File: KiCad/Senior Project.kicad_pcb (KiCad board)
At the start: 4 copper layers, 25 x 60 mm, 86 parts, among them J1 USB_C_Receptacle_USB2.0_16P, J2 Screw_Terminal_01x02, J3 Screw_Terminal_01x06, J4 Conn_ARM_JTAG_SWD_10, J5 Conn_01x02, Q2 IRLML0030, Q3 IRLML0030, Q4 IRLML0030, SW1 SW_Push, SW2 SW_Push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

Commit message: 3d model fixes
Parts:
- U4: value MS560702BA03-50 -> e
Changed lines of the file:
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@@
 		)
 		(embedded_fonts no)
+		(model "${KIPRJMOD}/3dmodels/IND_TAIYO_NR3015_TAY.step"
+			(offset
+				(xyz 0 0 0)
+			)
+			(scale
+				(xyz 1 1 1)
+			)
+			(rotate
+				(xyz -0 -0 -0)
+			)
+		)
 	)
 	(footprint "S3FH4R2:QFN40P700X700X90-57N"
@@
 		)
 		(embedded_fonts no)
+		(model "${KIPRJMOD}/3dmodels/ESP32-S3FH4R2.step"
+			(offset
+				(xyz 0 0 0)
+			)
+			(scale
+				(xyz 1 1 1)
+			)
+			(rotate
+				(xyz -90 -0 -0)
+			)
+		)
 	)
 	(footprint "Capacitor_SMD:C_0402_1005Metric"
@@
 		)
 		(embedded_fonts no)
-		(model "${KICAD9_3DMODEL_DIR}/Button_Switch_SMD.3dshapes/SW_SPST_PTS810.wrl"
+		(model "${KIPRJMOD}/3dmodels/PTS810SJM250SMTR LFS.STEP"
 			(offset
 				(xyz 0 0 0)
@@
 			)
 			(rotate
-				(xyz 0 0 0)
+				(xyz -90 -0 -0)
 			)
 		)
@@
 		)
 		(embedded_fonts no)
-		(model "${KICAD9_3DMODEL_DIR}/Button_Switch_SMD.3dshapes/SW_SPST_PTS810.wrl"
+		(model "${KIPRJMOD}/3dmodels/PTS810SJM250SMTR LFS.STEP"
 			(offset
 				(xyz 0 0 0)
@@
 			)
 			(rotate
-				(xyz 0 0 0)
+				(xyz -90 -0 -0)
 			)
 		)
@@
 			)
 		)
-		(property "Value" "MS560702BA03-50"
+		(property "Value" "e"
 			(at 0 0 0)
 			(unlocked yes)
@@
 		)
 		(embedded_fonts no)
+		(model "${KIPRJMOD}/3dmodels/MS560702BA03-50.STEP"
+			(offset
+				(xyz 0 0 1)
+			)
+			(scale
+				(xyz 1 1 1)
+			)
+			(rotate
+				(xyz -0 -0 -90)
+			)
+		)
 	)
 	(footprint "Resistor_SMD:R_0402_1005Metric"
@@
 		)
 		(embedded_fonts no)
-		(model "${KICAD9_3DMODEL_DIR}/RF_Module.3dshapes/HOPERF_RFM9XW_SMD.wrl"
+		(model "${KIPRJMOD}/3dmodels/RFM95W-915S2.STEP"
 			(offset
 				(xyz 0 0 0)
@@
 			)
 			(rotate
-				(xyz 0 0 0)
+				(xyz -90 -0 -0)
 			)
 		)
@@
 		)
 		(embedded_fonts no)
-		(model "${KICAD9_3DMODEL_DIR}/RF_Antenna.3dshapes/Molex_47948-0001_2.4Ghz.wrl"
+		(model "${KIPRJMOD}/3dmodels/0479480001.step"
 			(offset
-				(xyz 0 0 0)
+				(xyz 0 0 4)
 			)
 			(scale
@@
 			)
 			(rotate
-				(xyz 0 0 0)
+				(xyz -0 180 90)
 			)
 		)
@@
 		)
 		(embedded_fonts no)
-		(model "${KICAD9_3DMODEL_DIR}/RF_GPS.3dshapes/ublox_SAM-M8Q.wrl"
+		(model "${KIPRJMOD}/3dmodels/SAM-M10Q-00B.STEP"
 			(offset
 				(xyz 0 0 0)
@@
 			)
 			(rotate
-				(xyz 0 0 0)
+				(xyz -90 -0 -0)
 			)
 		)

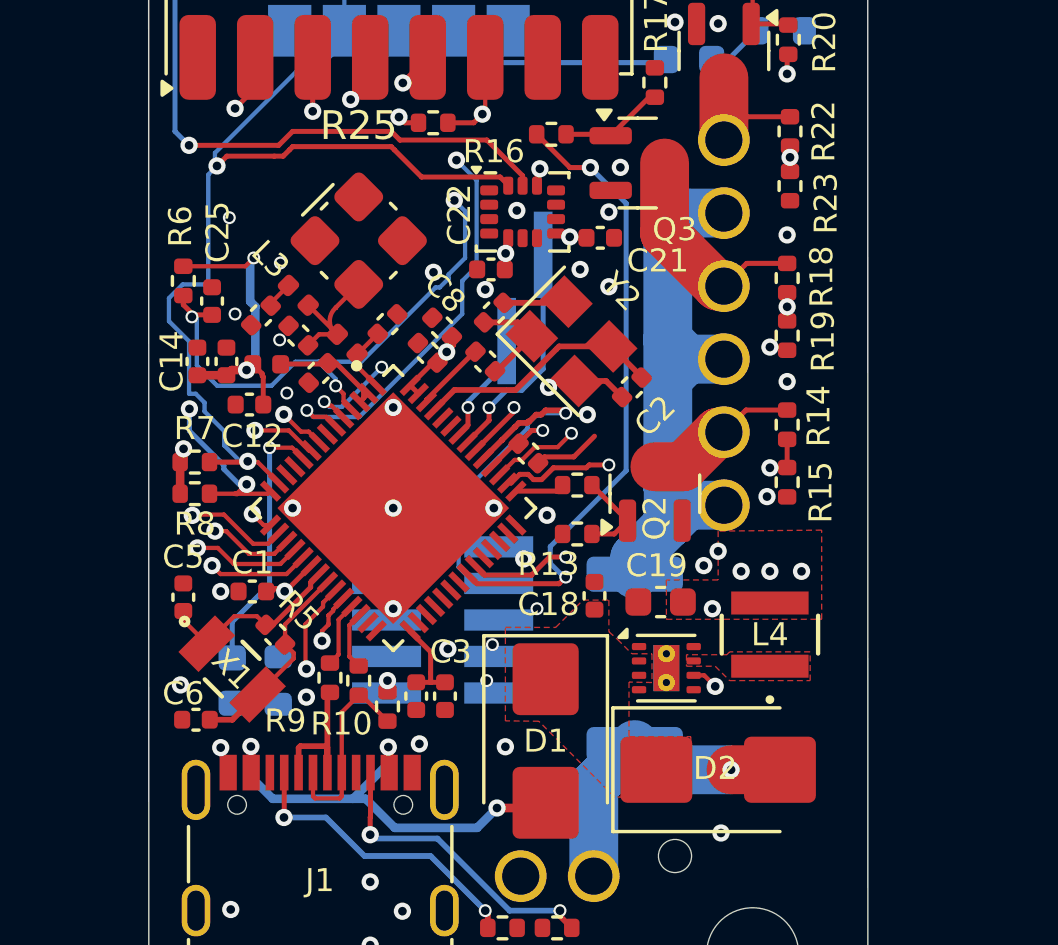
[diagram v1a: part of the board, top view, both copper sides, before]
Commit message: clean up schematic, add voltage dividers for measuring battery and charge firing current
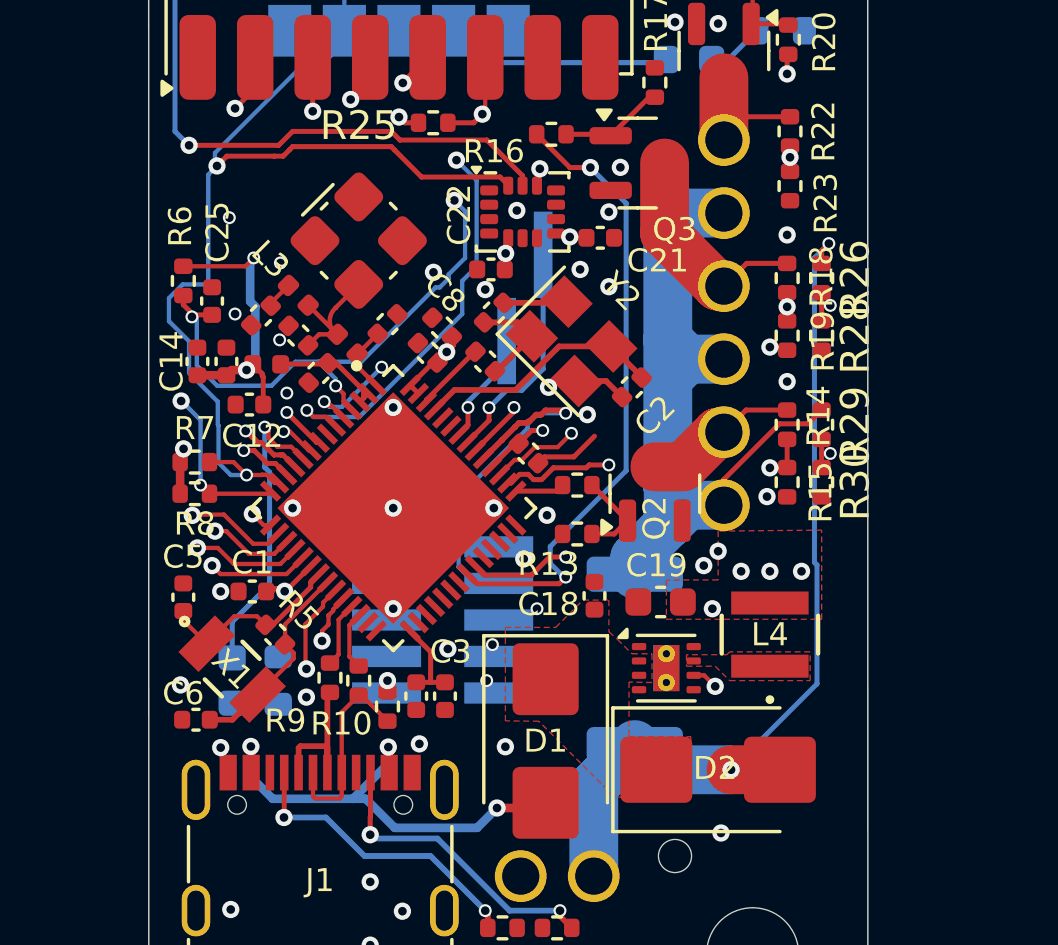
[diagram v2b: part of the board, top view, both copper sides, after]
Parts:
- added R26: 33k, Resistor_SMD:R_0402_1005Metric, F.Cu at (98.4, 89.5)
- added R28: 10k, Resistor_SMD:R_0402_1005Metric, F.Cu at (98.4, 91.5)
- added R29: 33k, Resistor_SMD:R_0402_1005Metric, F.Cu at (98.4, 94.6)
- added R30: 10k, Resistor_SMD:R_0402_1005Metric, F.Cu at (98.4, 96.6)
- U4: value e -> MS560702BA03-50
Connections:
- net /ESP-32 Power Coupler/VDD3P3 renamed Net-(U1-VDD3P3)
- net /LNA Shield/LNA_IN renamed /WiFi Antenna/LNA_IN
- net Net-(JP2-B) renamed /BOOT
- C3 pad 1: Net-(U1-VDD_SPI) -> +3V3
- C7 pad 1: Net-(U1-VDD_SPI) -> +3V3
- U1 pad 11: unconnected-(U1-GPIO6-Pad11) -> /BATTERY_SENSE
- U1 pad 12: unconnected-(U1-GPIO7-Pad12) -> /CURRENT_SENSE
- U1 pad 29: Net-(U1-VDD_SPI) -> +3V3
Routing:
- net /CURRENT_SENSE: track 0.00 -> 27.2 mm, vias 0 -> 2
- net /BATTERY_SENSE: track 0.00 -> 26.6 mm, vias 0 -> 2
- net +BATT: track 11.9 -> 32.4 mm, vias 1 -> 2
- net Net-(J3-Pin_1): track 21.0 -> 26.3 mm
- net Net-(U1-VDD_SPI): track 3.09 -> 0.00 mm
- net +3V3: track 69.0 -> 72.1 mm
- net /RADIO_RST: track 21.7 -> 19.8 mm
- net /POWER_LED: track 9.17 -> 10.6 mm
- net /SCL: track 65.1 -> 64.2 mm
- net /SDA: track 59.4 -> 58.6 mm
- net /FSPICS0: track 20.3 -> 20.8 mm

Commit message: finalize layout, again
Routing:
- net /SDA: track 58.6 -> 58.0 mm
- net GND: vias 62 -> 64
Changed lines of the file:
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@@
 		(tags "resistor")
 		(property "Reference" "R30"
-			(at 0 -1.17 90)
+			(at 2 0 90)
 			(layer "F.SilkS")
 			(effects
 				(font
-					(size 1 1)
+					(size 0.8 0.8)
 					(thickness 0.15)
 				)
@@
 		(tags "resistor")
 		(property "Reference" "R29"
-			(at 0 -1.17 90)
+			(at -0.35 -0.95 270)
 			(layer "F.SilkS")
 			(effects
 				(font
-					(size 1 1)
+					(size 0.8 0.8)
 					(thickness 0.15)
 				)
@@
 		(tags "resistor")
 		(property "Reference" "R23"
-			(at 0.6 -1.25 90)
+			(at 0.35 -1.2 90)
 			(layer "F.SilkS")
 			(effects
@@
 		(tags "resistor")
 		(property "Reference" "R26"
-			(at 0 -1.17 90)
+			(at -0.4 -0.95 90)
 			(layer "F.SilkS")
 			(effects
 				(font
-					(size 1 1)
+					(size 0.8 0.8)
 					(thickness 0.15)
 				)
@@
 		(tags "resistor")
 		(property "Reference" "R19"
-			(at 0.2 -1.25 90)
+			(at 0.25 0.9 90)
 			(layer "F.SilkS")
 			(effects
 				(font
-					(size 0.8 0.8)
+					(size 0.6 0.8)
 					(thickness 0.15)
 				)
@@
 			(effects
 				(font
-					(size 1 1)
+					(size 0.8 0.8)
 					(thickness 0.15)
 				)
@@
 		(tags "resistor")
 		(property "Reference" "R15"
-			(at 0.35 -1.17 90)
+			(at 2 0 270)
 			(layer "F.SilkS")
 			(effects
@@
 			(effects
 				(font
-					(size 1 1)
+					(size 0.8 0.8)
 					(thickness 0.15)
 				)
@@
 		(tags "resistor")
 		(property "Reference" "R28"
-			(at 0 -1.17 90)
+			(at 0.45 -0.95 90)
 			(layer "F.SilkS")
 			(effects
 				(font
-					(size 1 1)
+					(size 0.8 0.8)
 					(thickness 0.15)
 				)
@@
 		(tags "resistor")
 		(property "Reference" "R14"
-			(at -0.3 -1.1 90)
+			(at 0 0.9 270)
 			(layer "F.SilkS")
 			(effects
 				(font
-					(size 0.8 0.8)
+					(size 0.6 0.8)
 					(thickness 0.15)
 				)
@@
 		(tags "resistor")
 		(property "Reference" "R18"
-			(at -0.05 -1.2 90)
+			(at 0 0.9 90)
 			(layer "F.SilkS")
 			(effects
 				(font
-					(size 0.8 0.8)
+					(size 0.6 0.8)
 					(thickness 0.15)
 				)
@@
 		(effects
 			(font
-				(size 1 1)
+				(size 0.8 0.8)
 				(thickness 0.15)
 			)
@@
 		(effects
 			(font
-				(size 1 1)
+				(size 0.8 0.8)
 				(thickness 0.15)
 			)
@@
 	)
 	(via
+		(at 76.4 85.75)
+		(size 0.45)
+		(drill 0.3)
+		(layers "F.Cu" "B.Cu")
+		(free yes)
+		(net 2)
+	)
+	(via
 		(at 80.480264 104.074525)
 		(size 0.6)
@@
 	)
 	(via
+		(at 75.7 99.2)
+		(size 0.45)
+		(drill 0.3)
+		(layers "F.Cu" "B.Cu")
+		(free yes)
+		(net 2)
+	)
+	(via
 		(at 88.3 76.5)
 		(size 0.6)
@@
 	)
 	(segment
-		(start 77.4 93.8)
-		(end 76.4 92.8)
+		(start 77.85 96.35)
+		(end 77.425 95.925)
 		(width 0.15)
 		(layer "B.Cu")
@@
 	)
 	(segment
-		(start 77.0677 85.904602)
-		(end 77.371702 85.6006)
+		(start 81.8 80.9)
+		(end 81.8 79.5)
 		(width 0.15)
 		(layer "B.Cu")
@@
 	(segment
 		(start 76.178878 89.721122)
-		(end 77.021122 89.721122)
-		(width 0.15)
-		(layer "B.Cu")
-		(net 28)
-	)
-	(segment
-		(start 78.4 96.35)
-		(end 77.85 96.35)
+		(end 76.25 89.721122)
 		(width 0.15)
 		(layer "B.Cu")
@@
 	)
 	(segment
-		(start 77.85 96.35)
-		(end 77.425 95.925)
+		(start 81.024 82.076)
+		(end 81.8 81.3)
 		(width 0.15)
 		(layer "B.Cu")
@@
 	)
 	(segment
-		(start 75.7 90.2)
+		(start 75.9 90)
 		(end 76.178878 89.721122)
 		(width 0.15)
@@
 	(segment
 		(start 76.4 91.7)
-		(end 75.7 91)
+		(end 75.9 91.2)
 		(width 0.15)
 		(layer "B.Cu")
@@
 	)
 	(segment
-		(start 81.8 80.9)
-		(end 81.8 79.5)
+		(start 81.8 81.3)
+		(end 81.8 80.9)
 		(width 0.15)
 		(layer "B.Cu")
@@
 	)
 	(segment
-		(start 75.7 91)
-		(end 75.7 90.2)
+		(start 81.8 79.5)
+		(end 83.6 77.7)
 		(width 0.15)
 		(layer "B.Cu")
@@
 	)
 	(segment
-		(start 77.0677 89.674543)
-		(end 77.0677 85.904602)
+		(start 78.4 96.35)
+		(end 77.85 96.35)
 		(width 0.15)
 		(layer "B.Cu")
@@
 	)
 	(segment
-		(start 81.024 82.076)
-		(end 81.8 81.3)
+		(start 77.3 85.1477)
+		(end 80.3717 82.076)
 		(width 0.15)
 		(layer "B.Cu")
@@
 	)
 	(segment
-		(start 76.4 92.8)
-		(end 76.4 91.7)
-		(width 0.15)
+		(start 77.3 85.6006)
+		(end 77.371702 85.6006)
+		(width 0.175)
 		(layer "B.Cu")
 		(net 28)
 	)
 	(segment
-		(start 81.8 81.3)
-		(end 81.8 80.9)
+		(start 77.3 85.6006)
+		(end 77.3 85.1477)
 		(width 0.15)
 		(layer "B.Cu")
@@
 	)
 	(segment
-		(start 81.8 79.5)
-		(end 83.6 77.7)
+		(start 76.25 86.722302)
+		(end 77.371702 85.6006)
 		(width 0.15)
 		(layer "B.Cu")
@@
 	)
 	(segment
-		(start 77.3 85.1477)
-		(end 80.3717 82.076)
+		(start 76.25 89.721122)
+		(end 76.25 86.722302)
 		(width 0.15)
 		(layer "B.Cu")
@@
 	)
 	(segment
-		(start 77.3 85.6006)
-		(end 77.371702 85.6006)
-		(width 0.175)
+		(start 76.4 92.8)
+		(end 76.4 91.7)
+		(width 0.15)
 		(layer "B.Cu")
 		(net 28)
 	)
 	(segment
-		(start 77.3 85.6006)
-		(end 77.3 85.1477)
+		(start 75.9 91.2)
+		(end 75.9 90)
 		(width 0.15)
 		(layer "B.Cu")
@@
 	)
 	(segment
-		(start 77.021122 89.721122)
-		(end 77.0677 89.674543)
+		(start 77.4 93.8)
+		(end 76.4 92.8)
 		(width 0.15)
 		(layer "B.Cu")

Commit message: ordering, for real this time
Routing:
- net +3V3: track 72.1 -> 73.1 mm, vias 20 -> 21
- net GND: vias 64 -> 63
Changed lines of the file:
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@@
 		(end 99.000139 60)
 		(stroke
-			(width 0.05)
+			(width 0.001)
 			(type default)
 		)
@@
 		(end 100.007346 113)
 		(stroke
-			(width 0.05)
+			(width 0.001)
 			(type default)
 		)
@@
 	)
 	(gr_line
-		(start 92.11943 113.999999)
-		(end 75.999861 114)
+		(start 92.119569 113.999999)
+		(end 76 114)
 		(stroke
-			(width 0.05)
+			(width 0.001)
 			(type default)
 		)
@@
 	(gr_arc
 		(start 100.007346 113)
-		(mid 96.504002 116.975526)
-		(end 92.11943 114)
+		(mid 96.504019 116.975523)
+		(end 92.119439 114.000033)
 		(stroke
-			(width 0.05)
+			(width 0.001)
 			(type default)
 		)
@@
 		(end 100.000139 60.999861)
 		(stroke
-			(width 0.05)
+			(width 0.001)
 			(type default)
 		)
@@
 	)
 	(gr_line
-		(start 74.999861 113.000139)
-		(end 74.992654 61)
+		(start 75 113)
+		(end 74.992793 60.999861)
 		(stroke
-			(width 0.05)
+			(width 0.001)
 			(type default)
 		)
@@
 	)
 	(gr_arc
-		(start 75.999861 114)
-		(mid 75.292803 113.707156)
-		(end 74.999861 113.000139)
+		(start 75.9999 114)
+		(mid 75.292793 113.707107)
+		(end 74.9999 113)
 		(stroke
-			(width 0.05)
+			(width 0.001)
 			(type default)
 		)
@@
 		(end 82.88057 60)
 		(stroke
-			(width 0.05)
+			(width 0.001)
 			(type default)
 		)
@@
 		(layer "Cmts.User")
 		(pts
-			(xy 75 114) (xy 75 60)
-		)
-		(height -6.3)
-		(orientation 1)
-		(format
-			(prefix "")
-			(suffix "")
-			(units 3)
-			(units_format 0)
-			(precision 4)
-			(suppress_zeroes yes)
-		)
-		(style
-			(thickness 0.1)
-			(arrow_length 1.27)
-			(text_position_mode 0)
-			(arrow_direction outward)
-			(extension_height 0.58642)
-			(extension_offset 0.5)
-			(keep_text_aligned yes)
-		)
-		(gr_text "54"
-			(at 67.55 87 90)
-			(layer "Cmts.User")
-			(effects
-				(font
-					(size 1 1)
-					(thickness 0.15)
-				)
-			)
-		)
-	)
-	(dimension
-		(type orthogonal)
-		(layer "Cmts.User")
-		(pts
-			(xy 75 114) (xy 100 114)
+			(xy 74.999901 113.000139) (xy 100 114)
 		)
 		(height 8)
@@
 			(keep_text_aligned yes)
 		)
-		(gr_text "25"
-			(at 87.5 120.85 0)
+		(gr_text "25.0001"
+			(at 87.499951 119.850139 0)
 			(layer "Cmts.User")
 			(effects
@@
 		(layer "Cmts.User")
 		(pts
-			(xy 78.9 56.99) (xy 95.9 117)
+			(xy 78.997179 56.992655) (xy 95.988967 117.007331)
 		)
 		(height -18.18)
@@
 			(keep_text_aligned yes)
 		)
-		(gr_text "60.01"
-			(at 59.57 86.995 90)
+		(gr_text "60.0147"
+			(at 59.667179 86.999993 90)
 			(layer "Cmts.User")
 			(effects
@@
 	)
 	(via
-		(at 76.4 85.75)
+		(at 76.6 86)
 		(size 0.45)
 		(drill 0.3)
@@
 	)
 	(via
-		(at 75.7 99.2)
-		(size 0.45)
-		(drill 0.3)
-		(layers "F.Cu" "B.Cu")
-		(free yes)
-		(net 2)
-	)
-	(via
 		(at 88.3 76.5)
 		(size 0.6)
@@
 	)
 	(segment
+		(start 84.3 103.56)
+		(end 83.36 103.56)
+		(width 0.175)
+		(layer "F.Cu")
+		(net 3)
+	)
+	(segment
 		(start 90.22 88.1)
 		(end 89.670792 88.1)
@@
 	(segment
 		(start 84.8 103.56)
-		(end 84.8 103.24)
+		(end 84.8 103.4)
 		(width 0.175)
 		(layer "F.Cu")
@@
 	)
 	(segment
+		(start 83.36 103.56)
+		(end 83.3 103.5)
+		(width 0.175)
+		(layer "F.Cu")
+		(net 3)
+	)
+	(segment
 		(start 78.945 92.9)
 		(end 78.945 92.83)
@@
 	)
 	(segment
+		(start 84.8 103.4)
+		(end 84.8 103.24)
+		(width 0.175)
+		(layer "F.Cu")
+		(net 3)
+	)
+	(segment
 		(start 87.5 88.1125)
 		(end 87.5 88.551449)
@@
 	)
 	(via
+		(at 84.8 103.4)
+		(size 0.45)
+		(drill 0.3)
+		(layers "F.Cu" "B.Cu")
+		(net 3)
+	)
+	(via
 		(at 88.6 85.7)
 		(size 0.6)
@@
 	)
 	(segment
-		(start 77.425 94.625)
-		(end 77.4 94.6)
+		(start 76.4 92.8)
+		(end 76.4 91.7)
 		(width 0.15)
 		(layer "B.Cu")
@@
 	)
 	(segment
-		(start 77.85 96.35)
-		(end 77.425 95.925)
+		(start 75.9 91.2)
+		(end 75.9 90)
 		(width 0.15)
 		(layer "B.Cu")
@@
 	)
 	(segment
-		(start 81.8 80.9)
-		(end 81.8 79.5)
+		(start 76.25 87.4)
+		(end 77.371702 86.278298)
 		(width 0.15)
 		(layer "B.Cu")
@@
 	)
 	(segment
-		(start 76.178878 89.721122)
-		(end 76.25 89.721122)
+		(start 76.4 91.7)
+		(end 75.9 91.2)
+		(width 0.15)
+		(layer "B.Cu")
+		(net 28)
+	)
+	(segment
+		(start 81.8 80.9)
+		(end 81.8 79.5)
 		(width 0.15)
 		(layer "B.Cu")
@@
 	)
 	(segment
-		(start 75.9 90)
-		(end 76.178878 89.721122)
+		(start 81.8 81.3)
+		(end 81.8 80.9)
 		(width 0.15)
 		(layer "B.Cu")
@@
 	)
 	(segment
-		(start 76.4 91.7)
-		(end 75.9 91.2)
+		(start 77.425 94.625)
+		(end 77.4 94.6)
 		(width 0.15)
 		(layer "B.Cu")
@@
 	)
 	(segment
-		(start 81.8 81.3)
-		(end 81.8 80.9)
+		(start 78.4 96.35)
+		(end 77.85 96.35)
 		(width 0.15)
 		(layer "B.Cu")
@@
 	)
 	(segment
-		(start 77.425 95.925)
-		(end 77.425 94.625)
+		(start 77.4 93.8)
+		(end 76.4 92.8)
 		(width 0.15)
 		(layer "B.Cu")
@@
 	)
 	(segment
-		(start 81.8 79.5)
-		(end 83.6 77.7)
+		(start 77.371702 86.278298)
+		(end 77.371702 85.6006)
 		(width 0.15)
 		(layer "B.Cu")
@@
 	)
 	(segment
-		(start 78.4 96.35)
-		(end 77.85 96.35)
+		(start 81.8 79.5)
+		(end 83.6 77.7)
 		(width 0.15)
 		(layer "B.Cu")
@@
 	)
 	(segment
-		(start 77.3 85.6006)
-		(end 77.371702 85.6006)
-		(width 0.175)
+		(start 77.4 94.6)
+		(end 77.4 93.8)
+		(width 0.15)
 		(layer "B.Cu")
 		(net 28)
@@
 	(segment
 		(start 77.3 85.6006)
-		(end 77.3 85.1477)
-		(width 0.15)
+		(end 77.371702 85.6006)
+		(width 0.175)
 		(layer "B.Cu")
 		(net 28)
 	)
 	(segment
-		(start 76.25 86.722302)
-		(end 77.371702 85.6006)
+		(start 77.3 85.6006)
+		(end 77.3 85.1477)
 		(width 0.15)
 		(layer "B.Cu")
@@
 	)
 	(segment
-		(start 77.4 94.6)
-		(end 77.4 93.8)
+		(start 75.9 90)
+		(end 76.178878 89.721122)
 		(width 0.15)
 		(layer "B.Cu")
@@
 	)
 	(segment
-		(start 76.25 89.721122)
-		(end 76.25 86.722302)
+		(start 77.425 95.925)
+		(end 77.425 94.625)
 		(width 0.15)
 		(layer "B.Cu")
@@
 	)
 	(segment
-		(start 76.4 92.8)
-		(end 76.4 91.7)
+		(start 80.3717 82.076)
+		(end 81.024 82.076)
 		(width 0.15)
 		(layer "B.Cu")
@@
 	)
 	(segment
-		(start 75.9 91.2)
-		(end 75.9 90)
+		(start 76.25 89.721122)
+		(end 76.25 87.4)
 		(width 0.15)
 		(layer "B.Cu")
@@
 	)
 	(segment
-		(start 80.3717 82.076)
-		(end 81.024 82.076)
+		(start 76.178878 89.721122)
+		(end 76.25 89.721122)
 		(width 0.15)
 		(layer "B.Cu")
@@
 	)
 	(segment
-		(start 77.4 93.8)
-		(end 76.4 92.8)
+		(start 77.85 96.35)
+		(end 77.425 95.925)
 		(width 0.15)
 		(layer "B.Cu")
